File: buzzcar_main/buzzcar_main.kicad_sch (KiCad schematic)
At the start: 24 parts, among them J1 9V Battery Cap, J2 5V Buck, J3 3.3V Buck, J4 Motor_A, J5 Motor_B, J6 Video GME12864, J7 Audio Amp PAM8904, J8 8Ω Speaker, SW1 Main Power, SW2 SW_Push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

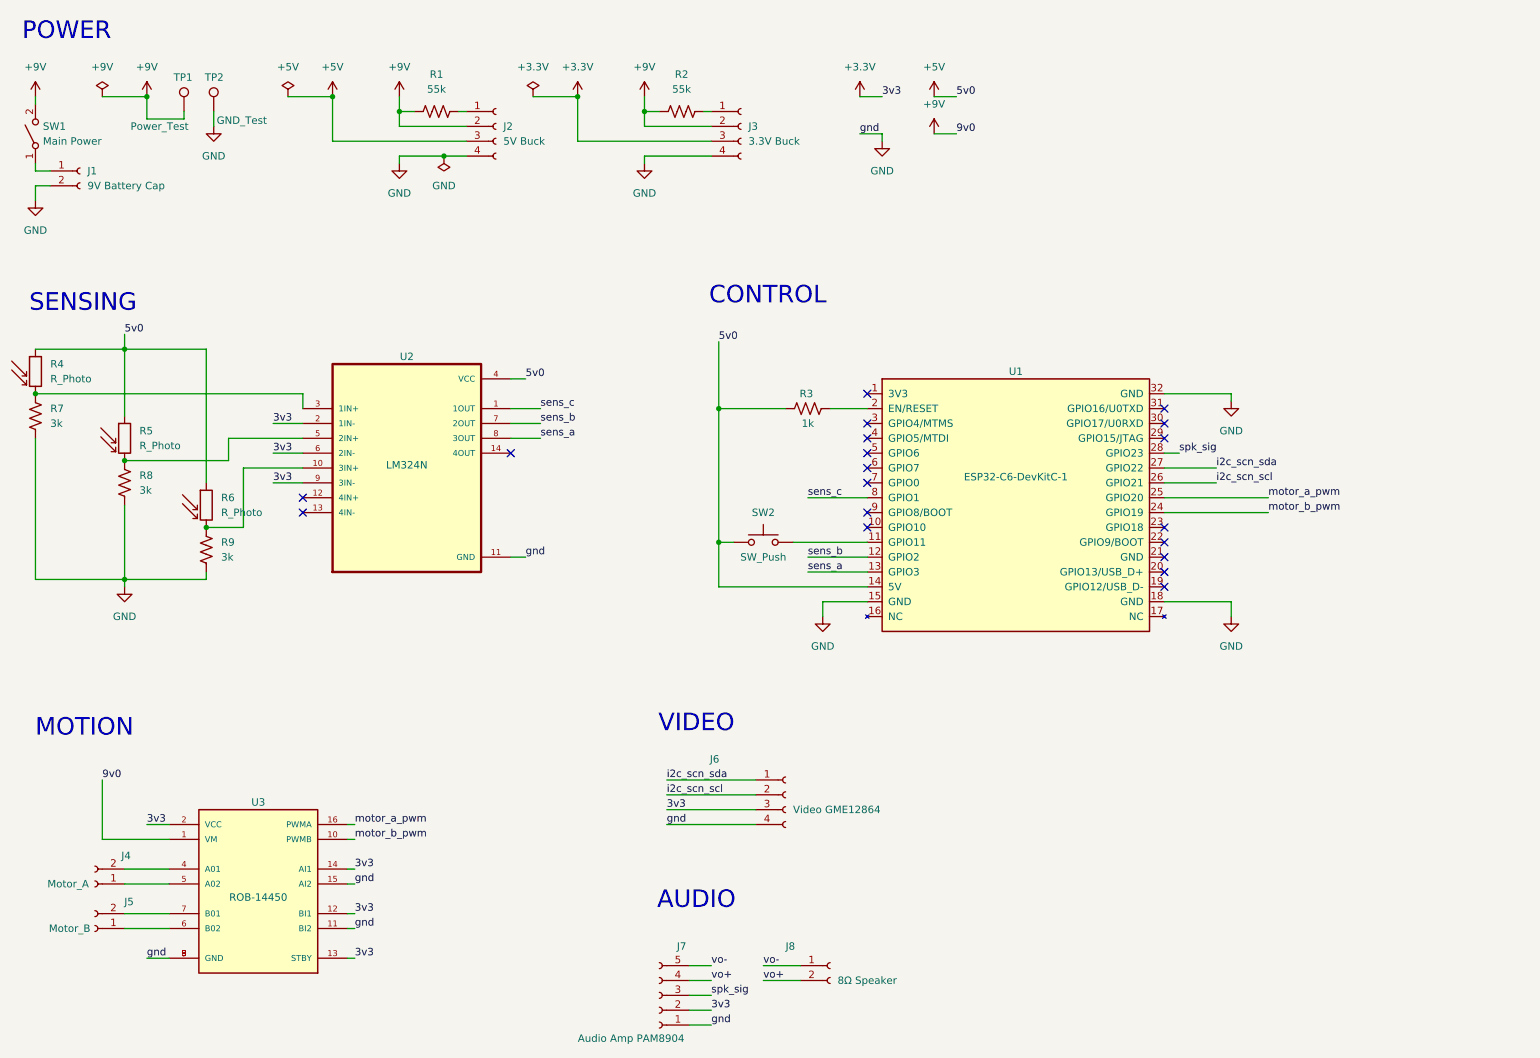
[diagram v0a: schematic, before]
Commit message: added leds, mounting and test pins to schematic
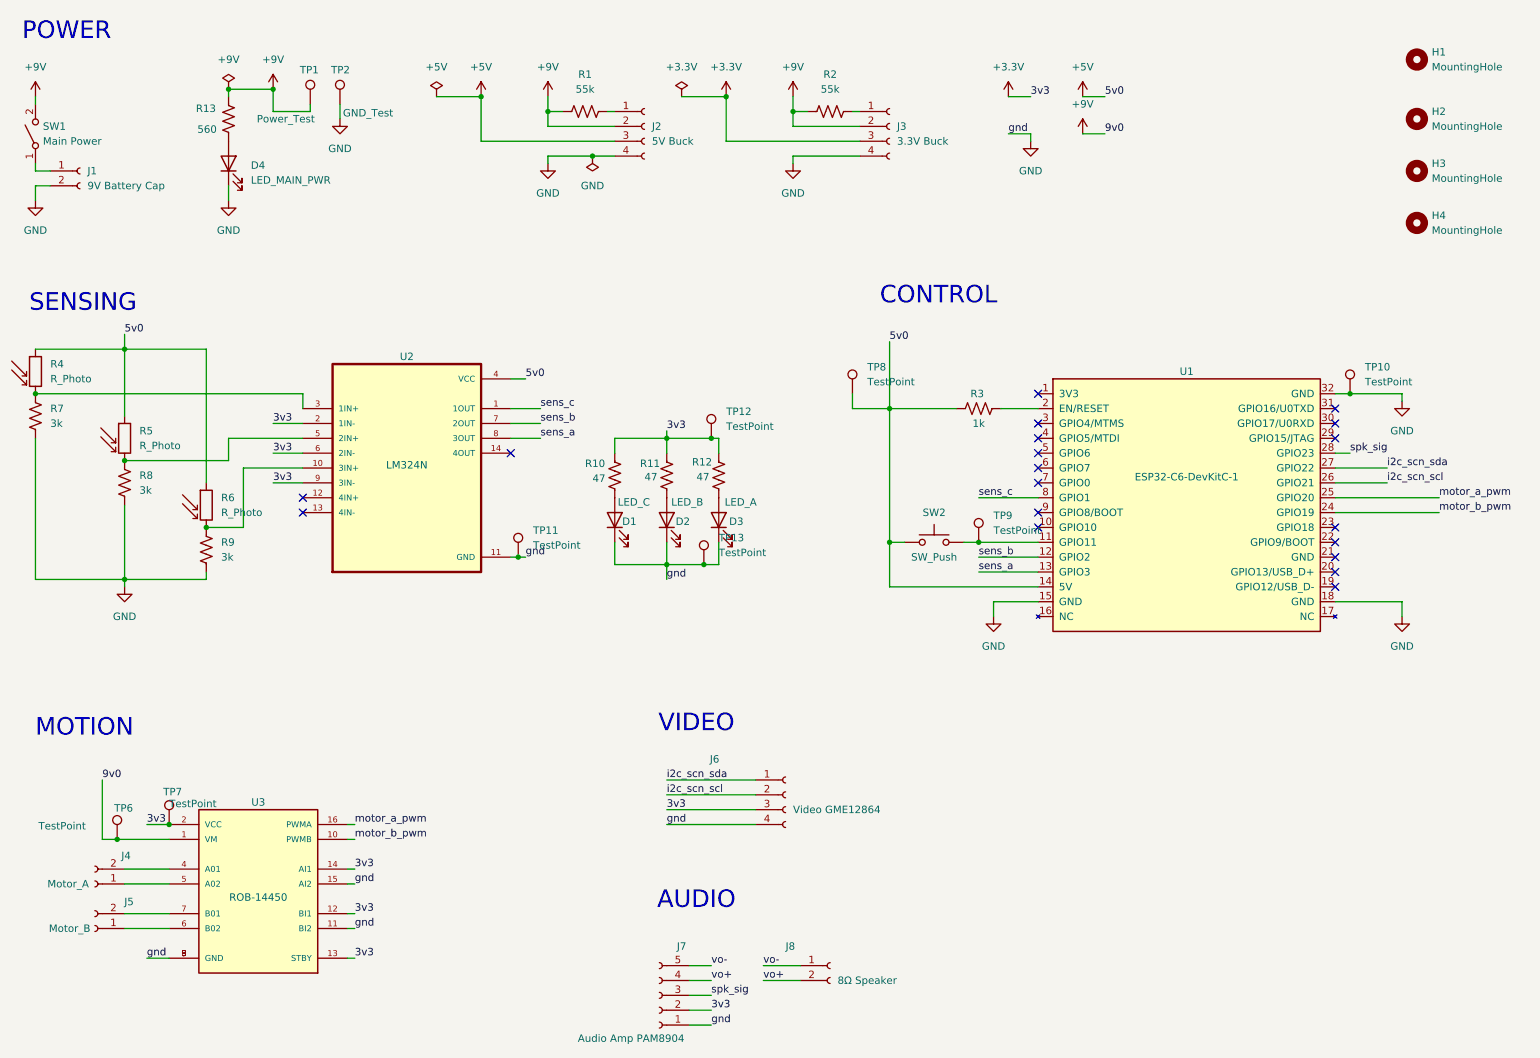
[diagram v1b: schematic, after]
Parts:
- added D1: LED_C, symbol Device:LED
- added D2: LED_B, symbol Device:LED
- added D3: LED_A, symbol Device:LED
- added D4: LED_MAIN_PWR, symbol Device:LED
- added H1, H2, H3, H4: MountingHole, symbol Mechanical:MountingHole
- added R10, R11, R12: 47, symbol Device:R_US
- added R13: 560, symbol Device:R_US
- added TP10, TP11, TP12, TP13, TP6, TP7, TP8, TP9: TestPoint, symbol Connector:TestPoint
- J2, J3, J6: footprint (none) -> Connector_PinHeader_2.54mm:PinHeader_1x04_P2.54mm_Vertical
- J7: footprint (none) -> Connector_PinHeader_2.54mm:PinHeader_1x05_P2.54mm_Vertical
- J8, SW1: footprint (none) -> Connector_PinHeader_2.54mm:PinHeader_1x02_P2.54mm_Vertical
- R1, R2, R3, R7, R8, R9: footprint (none) -> Resistor_THT:R_Axial_DIN0207_L6.3mm_D2.5mm_P10.16mm_Horizontal
- TP1, TP2: footprint (none) -> TestPoint:TestPoint_Loop_D2.60mm_Drill1.6mm_Beaded
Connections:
- net +3.3V: now also R10.1, R11.1, R12.1, TP12.1, TP7.1
- net +5V: now also TP8.1
- net +9V: now also R13.1, TP6.1
- net GND: now also D1.1 (K), D2.1 (K), D3.1 (K), D4.1 (K), TP10.1, TP11.1, TP13.1
- net at SW2.2, U1.11 (GPIO11): now also TP9.1
- new net: D3.2 (A), R12.2
- new net: D1.2 (A), R10.2
- new net: D4.2 (A), R13.2
- new net: D2.2 (A), R11.2
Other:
- moved on the sheet: J2, J3, R1, R2, R3, SW2, TP1, TP2, U1
